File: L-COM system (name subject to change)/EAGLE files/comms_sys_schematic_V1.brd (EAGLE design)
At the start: 43 x 72 mm, 49 parts, among them U1 R-78C5.0-1.0, U2 TLV75733PDBVR, X1 SMA-142-0701-801/806, Y1 ECS-TXO-2016-33-120-TR

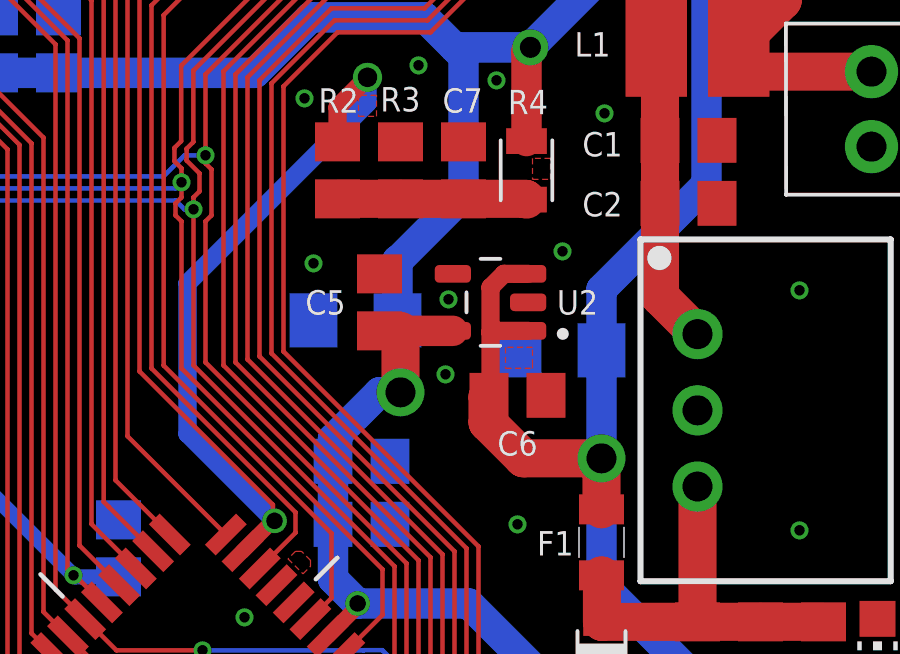
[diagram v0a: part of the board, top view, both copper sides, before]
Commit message: Replaced footprints for tantalum capacitors
Swapped out the tantalum capacitor's footprints for a slightly different one. Includes polarity marking on silkscreen.
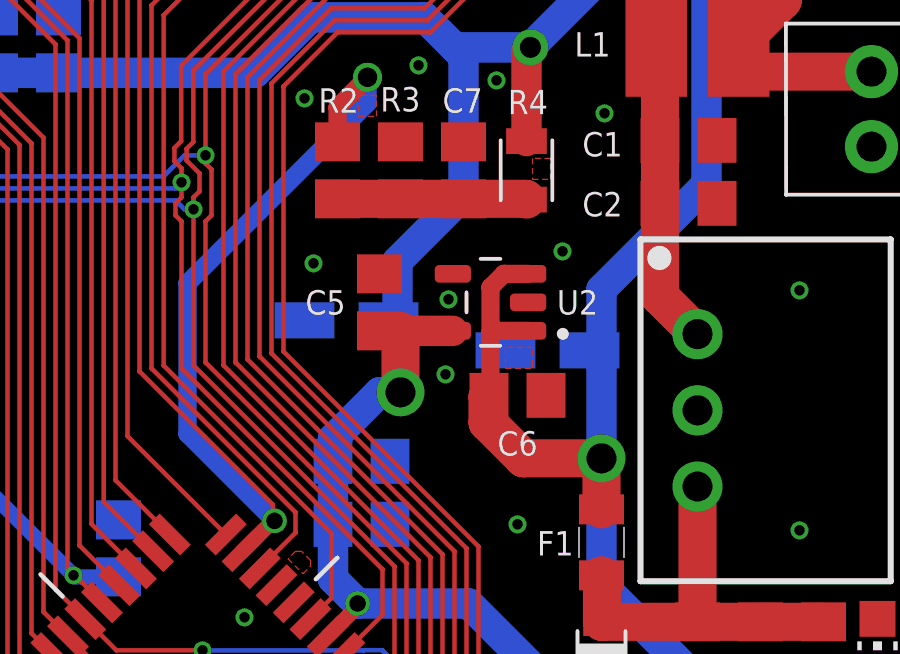
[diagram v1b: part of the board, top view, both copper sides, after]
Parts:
- C15, C9: value 10V 33uF Tant -> 10V 33uF tantalum; device rcl:C1206 -> rcl:CT3216
- moved C15 0.40 mm to (30.0, 53.0)
- moved C9 0.30 mm to (23.3, 54.0)
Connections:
- net +3.3V: now also C9.+; no longer C9.1
- net +5V: now also C15.+; no longer C15.1
- net GND: now also C15.-, C9.-; no longer C15.2, C9.2
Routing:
- net +5V: track 98.0 -> 98.6 mm
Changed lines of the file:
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@@
 <attribute name="SPICEPREFIX" value="C" x="15.7" y="46.4" size="1.778" layer="28" rot="MR90" display="off"/>
-</element>
-<element name="C9" library="rcl" library_urn="urn:adsk.eagle:library:334" package="C1206" package3d_urn="urn:adsk.eagle:package:23618/2" value="10V 33uF Tant" x="23.6" y="54" smashed="yes" rot="MR0">
-<attribute name="NAME" x="23.57" y="55.47" size="0.8128" layer="26" rot="MR0" align="center"/>
-<attribute name="POPULARITY" value="54" x="23.6" y="54" size="1.778" layer="28" rot="MR0" display="off"/>
-<attribute name="SPICEPREFIX" value="C" x="23.6" y="54" size="1.778" layer="28" rot="MR0" display="off"/>
-</element>
-<element name="C15" library="rcl" library_urn="urn:adsk.eagle:library:334" package="C1206" package3d_urn="urn:adsk.eagle:package:23618/2" value="10V 33uF Tant" x="30.4" y="53" smashed="yes" rot="MR0">
-<attribute name="NAME" x="30.37" y="54.57" size="0.8128" layer="26" rot="MR0" align="center"/>
-<attribute name="POPULARITY" value="54" x="30.4" y="53" size="1.778" layer="28" rot="MR0" display="off"/>
-<attribute name="SPICEPREFIX" value="C" x="30.4" y="53" size="1.778" layer="28" rot="MR0" display="off"/>
 </element>
 <element name="X1" library="con-coax" library_urn="urn:adsk.eagle:library:133" package="J502-ND-142-0701-801/806" package3d_urn="urn:adsk.eagle:package:6214/1" value="SMA-142-0701-801/806" x="-0.1" y="34.7" smashed="yes">
@@
 <attribute name="PACKAGE" value="0805 TE Connectivity" x="29.3" y="59" size="1.778" layer="27" rot="R270" display="off"/>
 <attribute name="PURCHASE-URL" value="https://pricing.snapeda.com/search/part/NTC0805J10K/?ref=eda" x="29.3" y="59" size="1.778" layer="27" rot="R270" display="off"/>
+</element>
+<element name="C9" library="rcl" library_urn="urn:adsk.eagle:library:334" package="CT3216" package3d_urn="urn:adsk.eagle:package:23327/2" value="10V 33uF tantalum" x="23.3" y="54" smashed="yes" rot="MR0">
+<attribute name="NAME" x="23.3" y="55.7" size="0.8128" layer="26" rot="MR0" align="center"/>
+<attribute name="POPULARITY" value="2" x="23.3" y="54" size="1.778" layer="28" rot="MR0" display="off"/>
+<attribute name="SPICEPREFIX" value="C" x="23.3" y="54" size="1.778" layer="28" rot="MR0" display="off"/>
+</element>
+<element name="C15" library="rcl" library_urn="urn:adsk.eagle:library:334" package="CT3216" package3d_urn="urn:adsk.eagle:package:23327/2" value="10V 33uF tantalum" x="30" y="53" smashed="yes" rot="MR0">
+<attribute name="NAME" x="30" y="54.7" size="0.8128" layer="26" rot="MR0" align="center"/>
+<attribute name="POPULARITY" value="2" x="30" y="53" size="1.778" layer="28" rot="MR0" display="off"/>
+<attribute name="SPICEPREFIX" value="C" x="30" y="53" size="1.778" layer="28" rot="MR0" display="off"/>
 </element>
 </elements>
@@
 <via x="18.4" y="36.3" extent="1-16" drill="0.35"/>
 <via x="17.1" y="39.7" extent="1-16" drill="0.35"/>
-<contactref element="C9" pad="2"/>
-<contactref element="C15" pad="2"/>
 <contactref element="X1" pad="G@1"/>
 <contactref element="X1" pad="G@4"/>
@@
 <via x="12.9" y="25.9" extent="1-16" drill="0.35"/>
 <via x="28.3" y="62" extent="1-16" drill="0.35"/>
+<contactref element="C9" pad="-"/>
+<contactref element="C15" pad="-"/>
 </signal>
 <signal name="+5V">
@@
 <wire x1="40.85" y1="6.35" x2="36.4" y2="1.9" width="1.016" layer="16"/>
 <wire x1="36.4" y1="1.9" x2="36.4" y2="1.5" width="1.016" layer="16"/>
-<contactref element="C15" pad="1"/>
-<wire x1="31.8" y1="55.03" x2="31.8" y2="53" width="1.016" layer="16"/>
-<wire x1="31.8" y1="53" x2="31.8" y2="49.4" width="1.016" layer="16"/>
 <wire x1="31.8" y1="47.7" x2="31.8" y2="49.4" width="1.27" layer="1"/>
 <wire x1="31.8" y1="49.4" x2="29.2" y2="49.4" width="1.27" layer="1"/>
@@
 <wire x1="28" y1="50.6" x2="28" y2="51.45" width="1.27" layer="1"/>
 <wire x1="28" y1="51.45" x2="28.05" y2="51.5" width="1.27" layer="1"/>
+<contactref element="C15" pad="+"/>
+<wire x1="31.8" y1="49.4" x2="31.8" y2="52.6" width="1.016" layer="16"/>
+<wire x1="31.8" y1="52.6" x2="31.4" y2="53" width="1.016" layer="16"/>
+<wire x1="31.8" y1="55.03" x2="31.8" y2="52.6" width="1.016" layer="16"/>
 </signal>
 <signal name="N$8">
@@
 <wire x1="24.4" y1="51.6" x2="22.85" y2="50.05" width="1.016" layer="16"/>
 <wire x1="22.85" y1="49.3" x2="22.85" y2="50.05" width="1.016" layer="16"/>
-<wire x1="25.1" y1="51.6" x2="24.4" y2="51.6" width="1.016" layer="16"/>
 <wire x1="22.85" y1="49.3" x2="22.85" y2="47.2" width="1.016" layer="16"/>
 <wire x1="34" y1="37.93149375" x2="27.3694" y2="44.56209375" width="1.016" layer="16"/>
@@
 <wire x1="22.85" y1="47.2" x2="22.85" y2="45.38149375" width="1.016" layer="16"/>
 <wire x1="22.85" y1="45.38149375" x2="23.6694" y2="44.56209375" width="1.016" layer="16"/>
-<contactref element="C9" pad="1"/>
-<wire x1="25" y1="54" x2="25" y2="51.7" width="1.016" layer="16"/>
-<wire x1="25" y1="51.7" x2="25.1" y2="51.6" width="1.016" layer="16"/>
-<wire x1="25" y1="54" x2="25" y2="56" width="1.016" layer="16"/>
-<wire x1="25.03" y1="56" x2="25" y2="56" width="1.016" layer="16"/>
 <wire x1="25.1" y1="51.6" x2="25.1" y2="53.65" width="1.27" layer="1"/>
 <wire x1="32" y1="36.45" x2="33.95" y2="36.45" width="1.27" layer="1"/>
@@
 <contactref element="R4" pad="1"/>
 <wire x1="22.1" y1="64.1" x2="25.9" y2="64.1" width="1.016" layer="16"/>
-<wire x1="27.2" y1="58.17" x2="25.03" y2="56" width="1.016" layer="16"/>
 <wire x1="25.9" y1="64.1" x2="26.9" y2="63.1" width="1.016" layer="16"/>
 <wire x1="26.9" y1="63.1" x2="27.2" y2="62.8" width="1.016" layer="16"/>
@@
 <wire x1="29.3" y1="62.97" x2="29.3" y2="59.975" width="1.016" layer="1"/>
 <via x="29.43" y="63.1" extent="1-16" drill="0.7" diameter="1.2"/>
+<contactref element="C9" pad="+"/>
+<wire x1="27.2" y1="58.17" x2="25" y2="55.97" width="1.016" layer="16"/>
+<wire x1="25.1" y1="51.6" x2="24.4" y2="51.6" width="1.016" layer="16"/>
+<wire x1="25.1" y1="51.6" x2="25.1" y2="53.6" width="1.016" layer="16"/>
+<wire x1="25" y1="53.7" x2="24.7" y2="54" width="1.016" layer="16"/>
+<wire x1="25" y1="55.97" x2="25" y2="53.7" width="1.016" layer="16"/>
+<wire x1="25" y1="53.7" x2="25.1" y2="53.6" width="1.016" layer="16"/>
 </signal>
 <signal name="PB1">
